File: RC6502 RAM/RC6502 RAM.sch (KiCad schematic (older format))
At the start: 23 parts, among them J3 RC6502_Backplane, U1 HM62256BLP-7, U2 74LS138, U3 74LS02, U4 74LS00, U5 74LS02

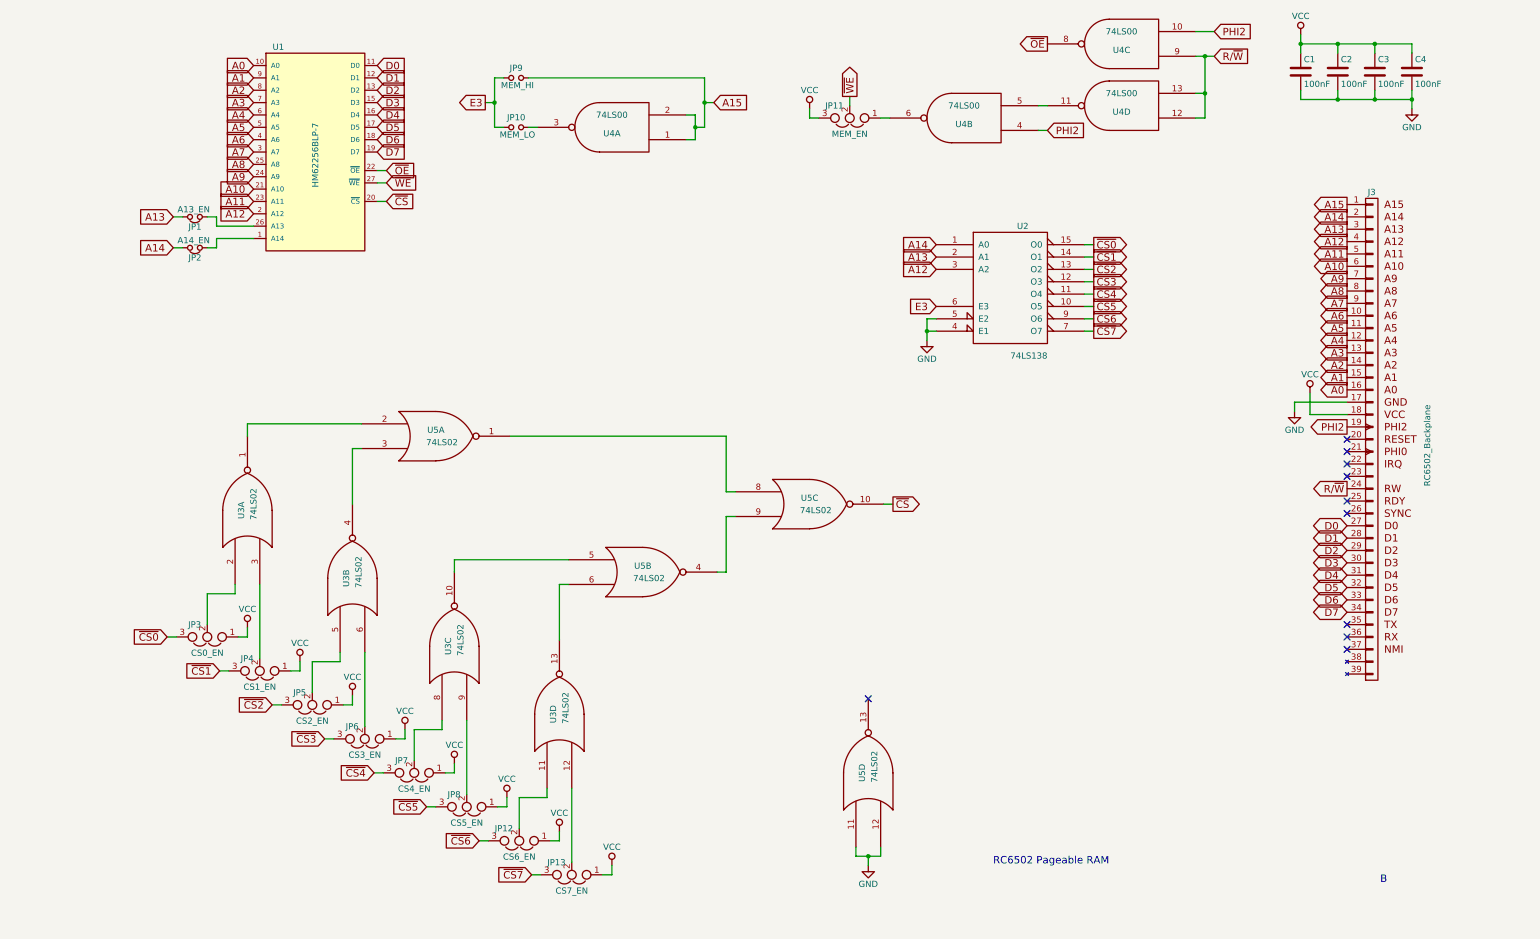
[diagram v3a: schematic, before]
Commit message: Enhanced RAM/ROM board, routing done
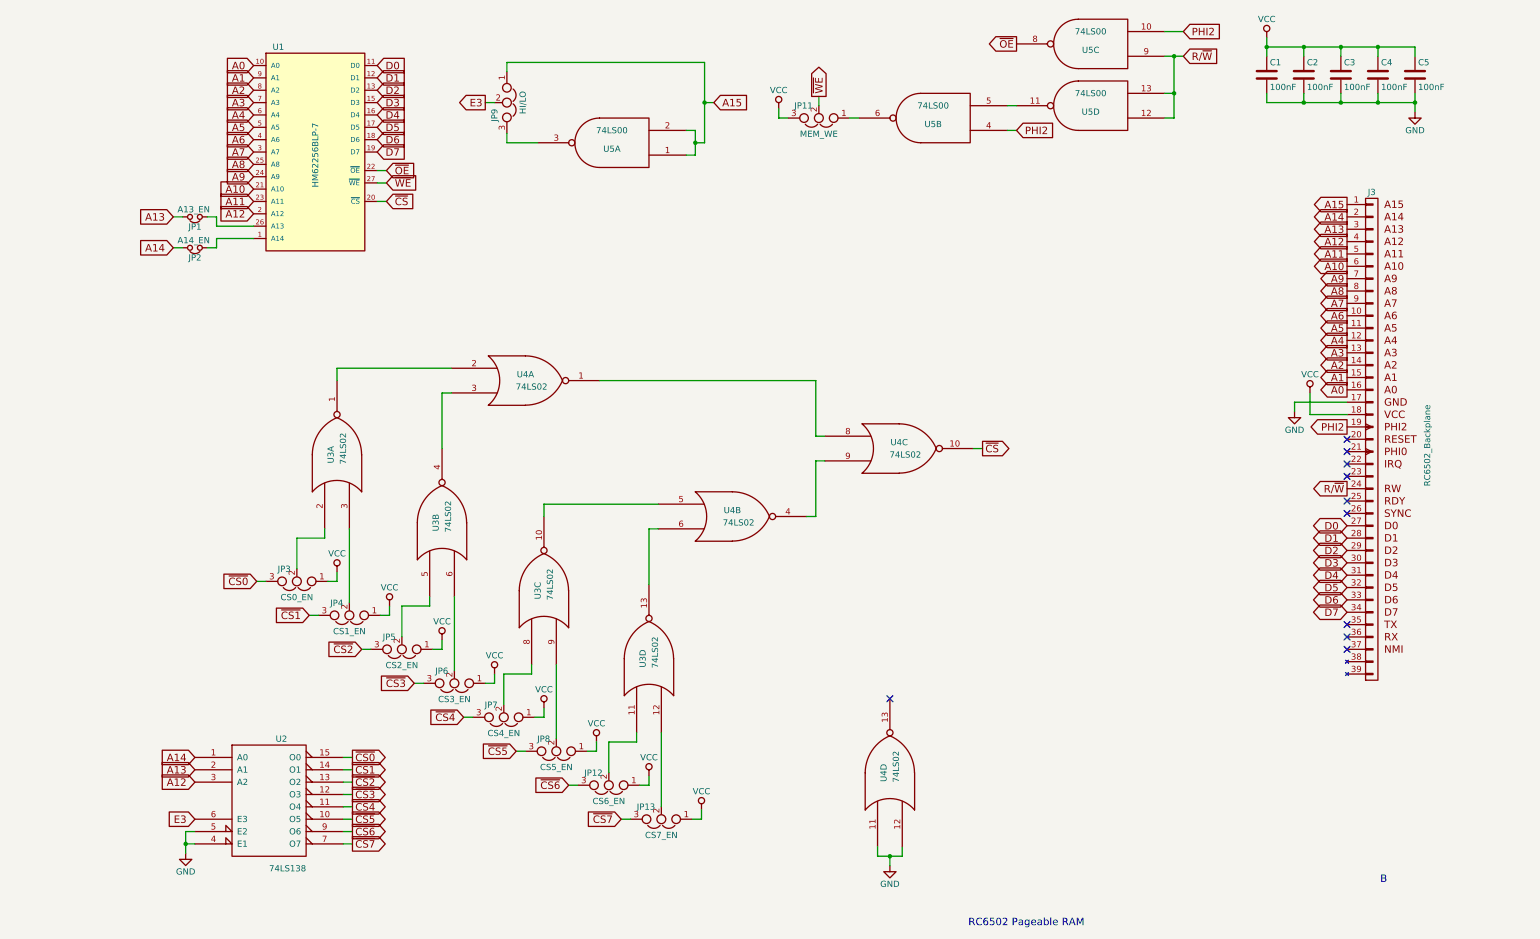
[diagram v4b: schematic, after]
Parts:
- removed JP10: MEM_LO, symbol Jumper_NO_Small
- removed JP9: MEM_HI, symbol Jumper_NO_Small
- added C5: 100nF, Capacitors_THT:C_Disc_D4.7mm_W2.5mm_P5.00mm, symbol C
- added JP9: HI/LO, Pin_Headers:Pin_Header_Straight_1x03_Pitch2.54mm, symbol Jumper_NC_Dual
- J3: footprint (none) -> Pin_Headers:Pin_Header_Angled_1x39_Pitch2.54mm
- JP1, JP2: footprint (none) -> Pin_Headers:Pin_Header_Straight_1x02_Pitch2.54mm
- JP11: value MEM_EN -> MEM_WE; footprint (none) -> Pin_Headers:Pin_Header_Straight_1x03_Pitch2.54mm
- JP12, JP13, JP3, JP4, JP5, JP6, JP7, JP8: footprint (none) -> Pin_Headers:Pin_Header_Straight_1x03_Pitch2.54mm
- U2: footprint (none) -> Housings_DIP:DIP-16_W7.62mm_Socket
- U3: footprint (none) -> Housings_DIP:DIP-14_W7.62mm_Socket
- U4: renamed from U5; footprint (none) -> Housings_DIP:DIP-14_W7.62mm_Socket
- U5: renamed from U4; footprint (none) -> Housings_DIP:DIP-14_W7.62mm_Socket
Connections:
- net A15: now also JP9.1
- net E3: now also JP9.2
- net GND: now also C5.2
- net VCC: now also C5.1
- net at U5.3: now also JP9.3
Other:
- moved on the sheet: C1, C2, C3, C4, JP11, JP12, JP13, JP3, JP4, JP5, JP6, JP7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

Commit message: Flipped decoder inputs, added details to silkscreen.
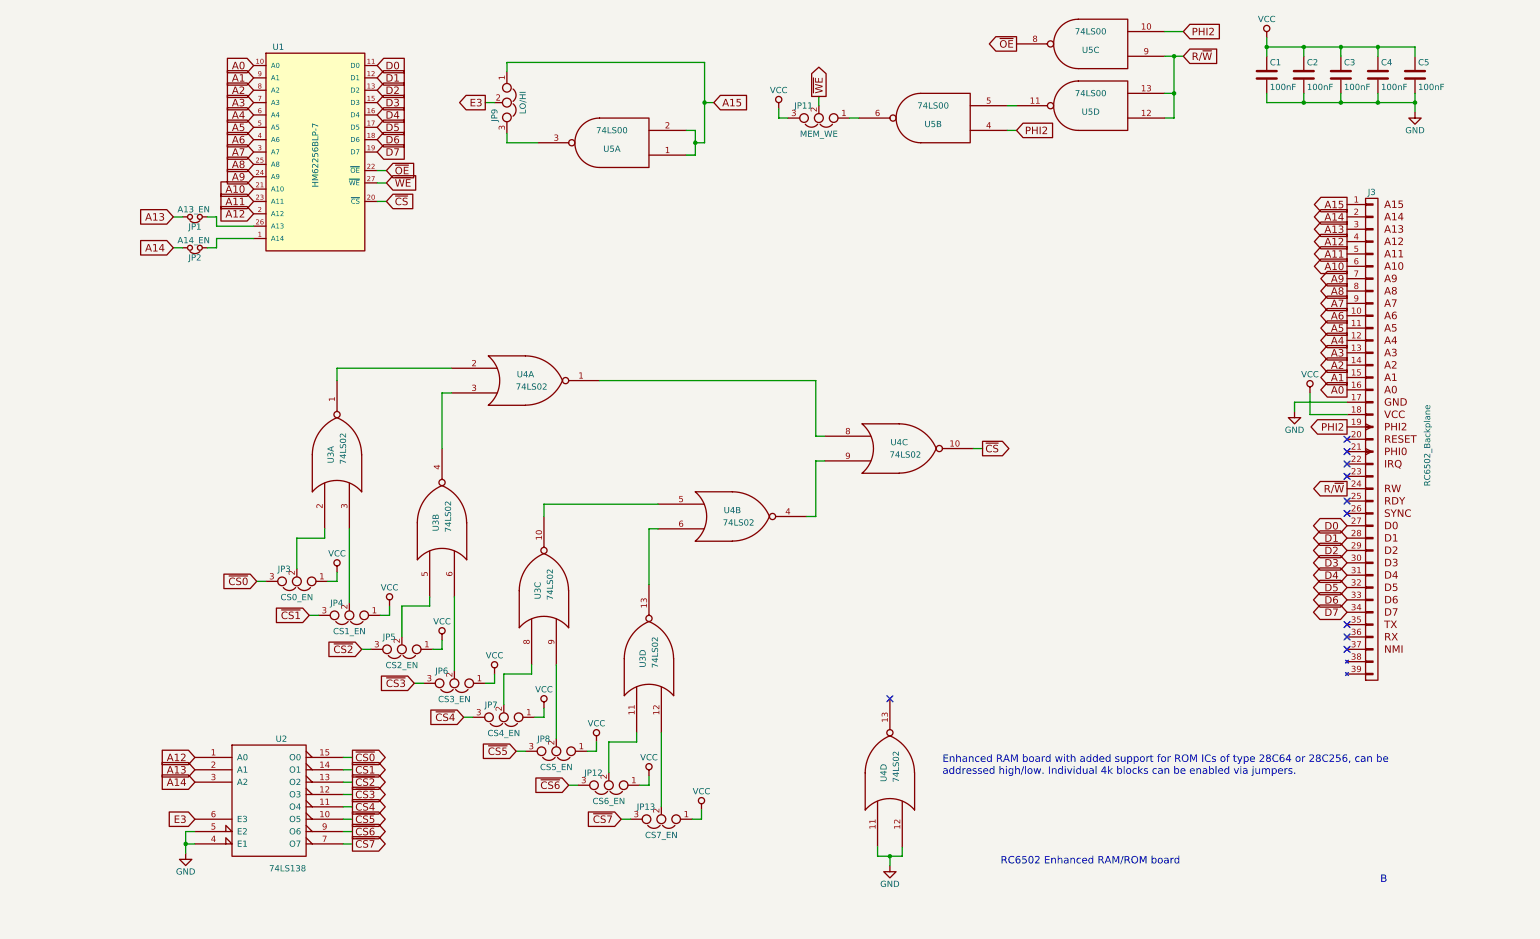
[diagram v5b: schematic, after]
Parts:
- JP9: value HI/LO -> LO/HI
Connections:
- net A12: now also U2.1 (A0); no longer U2.3 (A2)
- net A14: now also U2.3 (A2); no longer U2.1 (A0)
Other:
- note added: "Enhanced RAM board with added support for ROM ICs of type 28C64 or 28C256, can be\naddressed high/low. Individual 4k blocks can be enabled via jumpers."
- note added: "RC6502 Enhanced RAM/ROM board"
- note removed: "RC6502 Pageable RAM"
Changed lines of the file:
@@
 Text GLabel 1450 1025 0    60   Input ~ 0
 A0
-Text Notes 8175 8000 2    60   ~ 0
-RC6502 Pageable RAM
+Text Notes 8950 7500 2    60   ~ 0
+RC6502 Enhanced RAM/ROM board
 Text Notes 10625 7650 2    60   ~ 0
 B
@@
 	1    0    0    -1
 $EndComp
-Text GLabel 975  6625 0    60   Input ~ 0
+Text GLabel 975  6825 0    60   Input ~ 0
 A14
 Text GLabel 975  6725 0    60   Input ~ 0
 A13
-Text GLabel 975  6825 0    60   Input ~ 0
+Text GLabel 975  6625 0    60   Input ~ 0
 A12
 $Comp
@@
 P 3500 1325
 F 0 "JP9" H 3550 1225 50  0000 L CNN
-F 1 "HI/LO" H 3500 1425 50  0000 C BNN
+F 1 "LO/HI" H 3500 1425 50  0000 C BNN
 F 2 "Pin_Headers:Pin_Header_Straight_1x03_Pitch2.54mm" H 3500 1325 50  0001 C CNN
 F 3 "" H 3500 1325 50  0001 C CNN
@@
 	5100 1325 5175 1325
 Connection ~ 5100 1325
+Text Notes 7025 6775 0    60   ~ 0
+Enhanced RAM board with added support for ROM ICs of type 28C64 or 28C256, can be\naddressed high/low. Individual 4k blocks can be enabled via jumpers.
 $EndSCHEMATC
